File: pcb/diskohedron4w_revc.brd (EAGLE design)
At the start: 87.2 x 55.5 mm, 61 parts

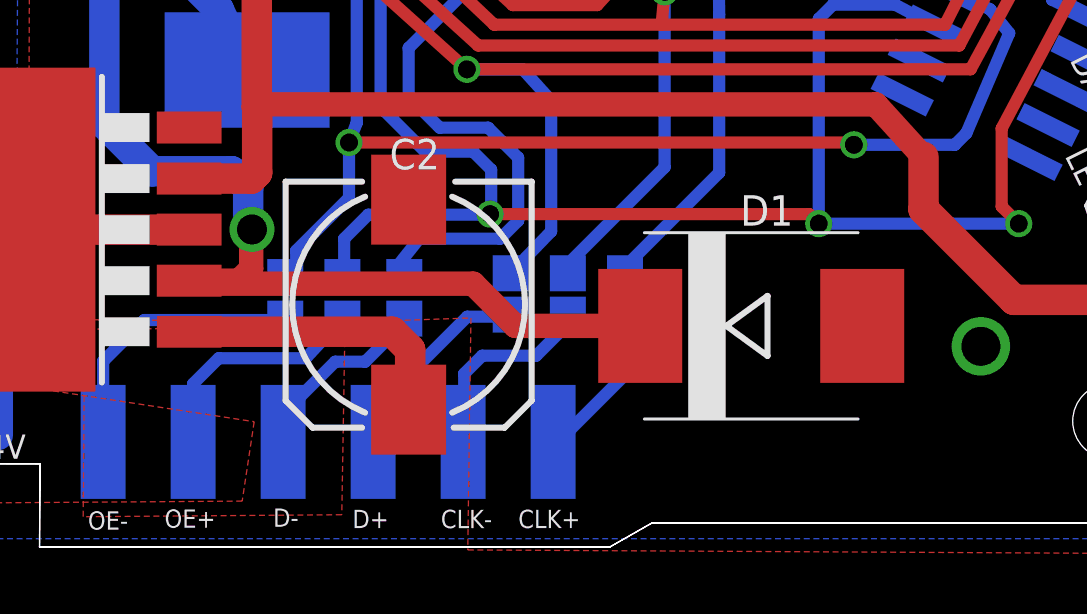
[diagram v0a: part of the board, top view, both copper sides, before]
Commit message: added termination resistors for rev.c & d
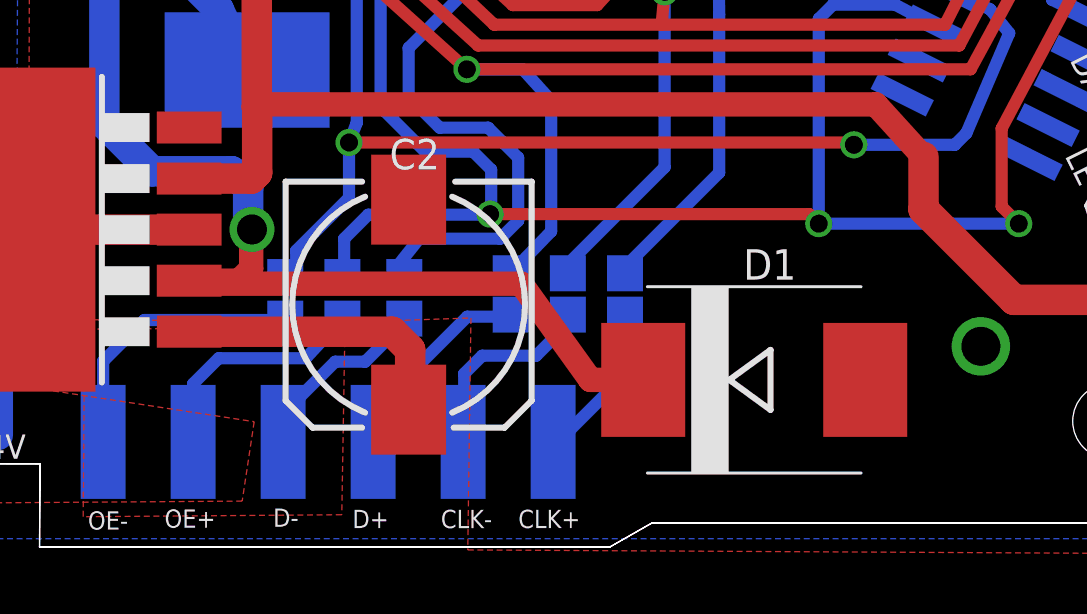
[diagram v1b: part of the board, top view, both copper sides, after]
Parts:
- moved D1 1.80 mm to (46.3, 4.79)
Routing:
- net N$2: track 42.9 -> 44.1 mm
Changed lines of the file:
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@@
 <?xml version="1.0" encoding="utf-8"?>
 <!DOCTYPE eagle SYSTEM "eagle.dtd">
-<eagle version="6.5.0">
+<eagle version="7.0.0">
 <drawing>
 <settings>
@@
 <layer number="17" name="Pads" color="2" fill="1" visible="yes" active="yes"/>
 <layer number="18" name="Vias" color="2" fill="1" visible="yes" active="yes"/>
-<layer number="19" name="Unrouted" color="6" fill="1" visible="no" active="yes"/>
+<layer number="19" name="Unrouted" color="6" fill="1" visible="yes" active="yes"/>
 <layer number="20" name="Dimension" color="15" fill="1" visible="yes" active="yes"/>
-<layer number="21" name="tPlace" color="7" fill="1" visible="no" active="yes"/>
+<layer number="21" name="tPlace" color="7" fill="1" visible="yes" active="yes"/>
 <layer number="22" name="bPlace" color="7" fill="1" visible="yes" active="yes"/>
-<layer number="23" name="tOrigins" color="15" fill="1" visible="no" active="yes"/>
+<layer number="23" name="tOrigins" color="15" fill="1" visible="yes" active="yes"/>
 <layer number="24" name="bOrigins" color="15" fill="1" visible="yes" active="yes"/>
-<layer number="25" name="tNames" color="7" fill="1" visible="no" active="yes"/>
+<layer number="25" name="tNames" color="7" fill="1" visible="yes" active="yes"/>
 <layer number="26" name="bNames" color="7" fill="1" visible="yes" active="yes"/>
-<layer number="27" name="tValues" color="7" fill="1" visible="no" active="yes"/>
-<layer number="28" name="bValues" color="7" fill="1" visible="no" active="yes"/>
+<layer number="27" name="tValues" color="7" fill="1" visible="yes" active="yes"/>
+<layer number="28" name="bValues" color="7" fill="1" visible="yes" active="yes"/>
 <layer number="29" name="tStop" color="7" fill="3" visible="no" active="yes"/>
 <layer number="30" name="bStop" color="7" fill="6" visible="no" active="yes"/>
@@
 <layer number="250" name="Descript" color="7" fill="1" visible="no" active="yes"/>
 <layer number="251" name="SMDround" color="7" fill="1" visible="no" active="yes"/>
-<layer number="253" name="geo_helper_axis" color="14" fill="1" visible="no" active="yes"/>
+<layer number="253" name="geo_helper_axis" color="14" fill="1" visible="yes" active="yes"/>
 <layer number="254" name="cooling" color="7" fill="1" visible="no" active="yes"/>
 <layer number="255" name="geo-helper" color="13" fill="1" visible="no" active="yes"/>
@@
 <pass name="Default">
 <param name="RoutingGrid" value="0.3mm"/>
+<param name="AutoGrid" value="1"/>
+<param name="Efforts" value="0"/>
+<param name="TopRouterVariant" value="1"/>
 <param name="tpViaShape" value="round"/>
 <param name="PrefDir.1" value="/"/>
@@
 </element>
 <element name="L1" library="inductors" package="DR127" value="30uH" x="29.365028125" y="20.096415625" smashed="yes" rot="MR270"/>
-<element name="D1" library="eagle-ltspice" package="DIODE_SMC" value="1N5824 3A" x="46.16789375" y="6.593409375" smashed="yes">
-<attribute name="SPICEMODEL" value="diode" x="46.16789375" y="6.593409375" size="1.778" layer="27" display="off"/>
-<attribute name="SPICEPREFIX" value="D" x="46.16789375" y="6.593409375" size="1.778" layer="27" display="off"/>
-<attribute name="NAME" x="45.80389375" y="9.934909375" size="1.016" layer="25"/>
+<element name="D1" library="eagle-ltspice" package="DIODE_SMC" value="1N5824 3A" x="46.26789375" y="4.793409375" smashed="yes">
+<attribute name="SPICEMODEL" value="diode" x="46.26789375" y="4.793409375" size="1.778" layer="27" display="off"/>
+<attribute name="SPICEPREFIX" value="D" x="46.26789375" y="4.793409375" size="1.778" layer="27" display="off"/>
+<attribute name="NAME" x="45.90389375" y="8.134909375" size="1.016" layer="25"/>
 </element>
 <element name="JP1" library="SparkFun-Connectors" package="1X05" value="EXTBRD" x="63.4040375" y="19.644678125" smashed="yes" rot="R243"/>
@@
 <wire x1="29.365028125" y1="25.071415625" x2="25.071415625" y2="25.071415625" width="1.016" layer="16"/>
 <wire x1="25.071415625" y1="25.071415625" x2="24.60625" y2="24.60625" width="1.016" layer="16"/>
-<wire x1="42.46789375" y1="6.593409375" x2="38.306590625" y2="6.593409375" width="0.8128" layer="1"/>
-<wire x1="38.306590625" y1="6.593409375" x2="36.9" y2="8" width="0.8128" layer="1"/>
-<wire x1="36.9" y1="8" x2="27.53373125" y2="8" width="0.8128" layer="1"/>
+<wire x1="42.56789375" y1="4.793409375" x2="40.806590625" y2="4.793409375" width="0.8128" layer="1"/>
+<wire x1="40.806590625" y1="4.793409375" x2="38.5" y2="8" width="0.8128" layer="1"/>
+<wire x1="38.5" y1="8" x2="27.53373125" y2="8" width="0.8128" layer="1"/>
 <wire x1="27.53373125" y1="8" x2="27.433446875" y2="8.100284375" width="0.8128" layer="1"/>
 <wire x1="27.433446875" y1="8.100284375" x2="29.100284375" y2="8.100284375" width="0.8128" layer="1"/>
